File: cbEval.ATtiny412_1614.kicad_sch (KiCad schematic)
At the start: 50 parts, among them J1 Bergstik-II_3, J10 Socket.Hor.2x5.6-5535512-4, J11 Bergstik-II_3, J12 Bergstik-II_3, J13 Bergstik-II_6, J14 Bergstik-II_6, J15 Bergstik-II_6, J16 Bergstik-II_3, J17 Bergstik-II_6, J18 Bergstik-II_3, J19 Bergstik-II_6, J2 Bergstik-II_6, J20 Bergstik-II_3, J21 Bergstik-II_3, J22 Bergstik-II_2, J23 Bergstik-II_2, J3 Keystone.4918, J4 Keystone.4918, J5 Keystone.3571, J6 Keystone.3571, J7 Socket.Hor.2x5.6-5535512-4, J8 Header.Hor.2x5.9-103326-0-05, J9 Header.Hor.2x5.9-103326-0-05, U1 ATtiny412-SSFR, U2 ATtiny1614-SSFR

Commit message: kleinere Änderungen
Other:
- moved on the sheet: J23
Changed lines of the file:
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@@
   (junction (at 238.76 129.54) (diameter 0.9144) (color 0 0 0 0))
   (junction (at 251.46 50.8) (diameter 0.9144) (color 0 0 0 0))
-  (junction (at 266.7 144.78) (diameter 0.9144) (color 0 0 0 0))
   (junction (at 274.32 144.78) (diameter 0.9144) (color 0 0 0 0))
   (no_connect (at 68.58 17.78))
@@
     (stroke (width 0) (type solid) (color 0 0 0 0))
   )
+  (wire (pts (xy 137.16 99.06) (xy 127 99.06))
+    (stroke (width 0) (type solid) (color 0 0 0 0))
+  )
+  (wire (pts (xy 137.16 101.6) (xy 137.16 99.06))
+    (stroke (width 0) (type solid) (color 0 0 0 0))
+  )
   (wire (pts (xy 139.7 35.56) (xy 139.7 38.1))
     (stroke (width 0) (type solid) (color 0 0 0 0))
@@
     (stroke (width 0) (type solid) (color 0 0 0 0))
   )
-  (wire (pts (xy 139.7 99.06) (xy 127 99.06))
+  (wire (pts (xy 139.7 99.06) (xy 149.86 99.06))
     (stroke (width 0) (type solid) (color 0 0 0 0))
   )
@@
     (stroke (width 0) (type solid) (color 0 0 0 0))
   )
-  (wire (pts (xy 142.24 99.06) (xy 149.86 99.06))
-    (stroke (width 0) (type solid) (color 0 0 0 0))
-  )
-  (wire (pts (xy 142.24 101.6) (xy 142.24 99.06))
-    (stroke (width 0) (type solid) (color 0 0 0 0))
-  )
   (wire (pts (xy 147.32 165.1) (xy 154.94 165.1))
     (stroke (width 0) (type solid) (color 0 0 0 0))
@@
     (stroke (width 0) (type solid) (color 0 0 0 0))
   )
-  (wire (pts (xy 264.16 144.78) (xy 266.7 144.78))
-    (stroke (width 0) (type solid) (color 0 0 0 0))
-  )
   (wire (pts (xy 266.7 144.78) (xy 274.32 144.78))
     (stroke (width 0) (type solid) (color 0 0 0 0))
@@
     (stroke (width 0) (type solid) (color 0 0 0 0))
   )
-  (wire (pts (xy 274.32 147.32) (xy 274.32 144.78))
+  (wire (pts (xy 274.32 144.78) (xy 274.32 147.32))
     (stroke (width 0) (type solid) (color 0 0 0 0))
   )
@@
     (pin "2")
   )
-  (symbol (lib_id "J.PinHeader:Bergstik-II_2") (at 142.24 106.68 90) (mirror x) (unit 1)
-    (in_bom yes) (on_board yes)
-    (property "Reference" "J23" (id 0) (at 142.24 121.92 90))
-    (property "Value" "Bergstik-II_2" (id 1) (at 142.24 119.38 90))
-    (property "Footprint" "Connector_PinHeader_2.54mm:PinHeader_1x02_P2.54mm_Vertical" (id 2) (at 139.7 114.3 90)
-      (effects (font (size 1.27 1.27)) hide)
-    )
-    (property "Datasheet" "https://cdn.amphenol-icc.com/media/wysiwyg/files/drawing/68000.pdf?__cf_chl_jschl_tk__=264da0a199af1bdefb04026963ad3c85a073036f-1615910483-0-AaX8LtgG8apEDzGIqgzQ0aoAKWkj50oj4JyeD-4a-BjpVTotUkz0b9CwK48SctxW9RfQ29uHK-g8U4Q7W950UfkLI47M2h-zbxXP0QVGLOROToQCZGWcFC-c_QilEUacZTRKDvvL4FAsQqyycsf3m4Eg-isf3_QP12ONd_wWQcMNK-LuQ3eyU0ZB_uGz-1tHBPJYyv3B6ZQ-xQw3v8oWI_eE_zzEWbIWrLFoFf6eZXoAoT5Y4wJiyDXoV-vBmq5F4mSG8H7EqnWkU4EpxDA2-swokem-Q60MTknd4E9RK0nSmJU_PhEDac0Sb3Im75HD1QHXcTu1yMJzQCNpgpofH-wmgz79VfPk4ttpW38ZPDdPIxv_B7gR4gWWdhvgQyW6byYqLE8E5a8tpA31lZkCN19ufDO8SqP6UAFJscCeeydKEgOe2Ksu_LJQubib6v3-6A" (id 3) (at 139.7 116.84 90)
-      (effects (font (size 1.27 1.27)) hide)
-    )
-    (property "Package" "1x2-2.54" (id 4) (at 142.24 116.84 90))
-    (property "Usage" "LEDs" (id 5) (at 142.24 114.3 90))
-    (property "ID" "68000-102HLF" (id 6) (at 140.97 110.49 90)
-      (effects (font (size 0.635 0.635)))
-    )
+  (symbol (lib_id "J.PinHeader:Bergstik-II_2") (at 139.7 106.68 90) (mirror x) (unit 1)
+    (in_bom yes) (on_board yes)
+    (property "Reference" "J23" (id 0) (at 139.7 121.92 90))
+    (property "Value" "Bergstik-II_2" (id 1) (at 139.7 119.38 90))
+    (property "Footprint" "Connector_PinHeader_2.54mm:PinHeader_1x02_P2.54mm_Vertical" (id 2) (at 137.16 114.3 90)
+      (effects (font (size 1.27 1.27)) hide)
+    )
+    (property "Datasheet" "https://cdn.amphenol-icc.com/media/wysiwyg/files/drawing/68000.pdf?__cf_chl_jschl_tk__=264da0a199af1bdefb04026963ad3c85a073036f-1615910483-0-AaX8LtgG8apEDzGIqgzQ0aoAKWkj50oj4JyeD-4a-BjpVTotUkz0b9CwK48SctxW9RfQ29uHK-g8U4Q7W950UfkLI47M2h-zbxXP0QVGLOROToQCZGWcFC-c_QilEUacZTRKDvvL4FAsQqyycsf3m4Eg-isf3_QP12ONd_wWQcMNK-LuQ3eyU0ZB_uGz-1tHBPJYyv3B6ZQ-xQw3v8oWI_eE_zzEWbIWrLFoFf6eZXoAoT5Y4wJiyDXoV-vBmq5F4mSG8H7EqnWkU4EpxDA2-swokem-Q60MTknd4E9RK0nSmJU_PhEDac0Sb3Im75HD1QHXcTu1yMJzQCNpgpofH-wmgz79VfPk4ttpW38ZPDdPIxv_B7gR4gWWdhvgQyW6byYqLE8E5a8tpA31lZkCN19ufDO8SqP6UAFJscCeeydKEgOe2Ksu_LJQubib6v3-6A" (id 3) (at 137.16 116.84 90)
+      (effects (font (size 1.27 1.27)) hide)
+    )
+    (property "Package" "1x2-2.54" (id 4) (at 139.7 116.84 90))
+    (property "Usage" "LEDs" (id 5) (at 139.7 114.3 90))
+    (property "ID" "68000-102HLF" (id 6) (at 138.43 110.49 90)
+      (effects (font (size 0.635 0.635)))
+    )

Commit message: BOM erstellt und kleinere Korrekturen
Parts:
- added R10, R11, R12, R13, R14, R15, R9: 10k, Resistor_SMD:R_0805_2012Metric, symbol R.Yageo.RC0805:10k
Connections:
- net GND: now also R10.2, R11.2, R12.2, R13.2, R14.2, R9.2
- net SPI-ADR0: now also R9.1
- net SPI-ADR1: now also R10.1
- net SPI-ADR2: now also R11.1
- net SPI-CLK: now also R14.1
- net SPI-MRST: now also R13.1
- net SPI-MTSR: now also R12.1
- net SPI-~CE: now also R15.2
- net VCC: now also R15.1
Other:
- moved on the sheet: D1A, D1B, H2, H3, J10, J13, J22, J23, R5, R6, R7, R8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

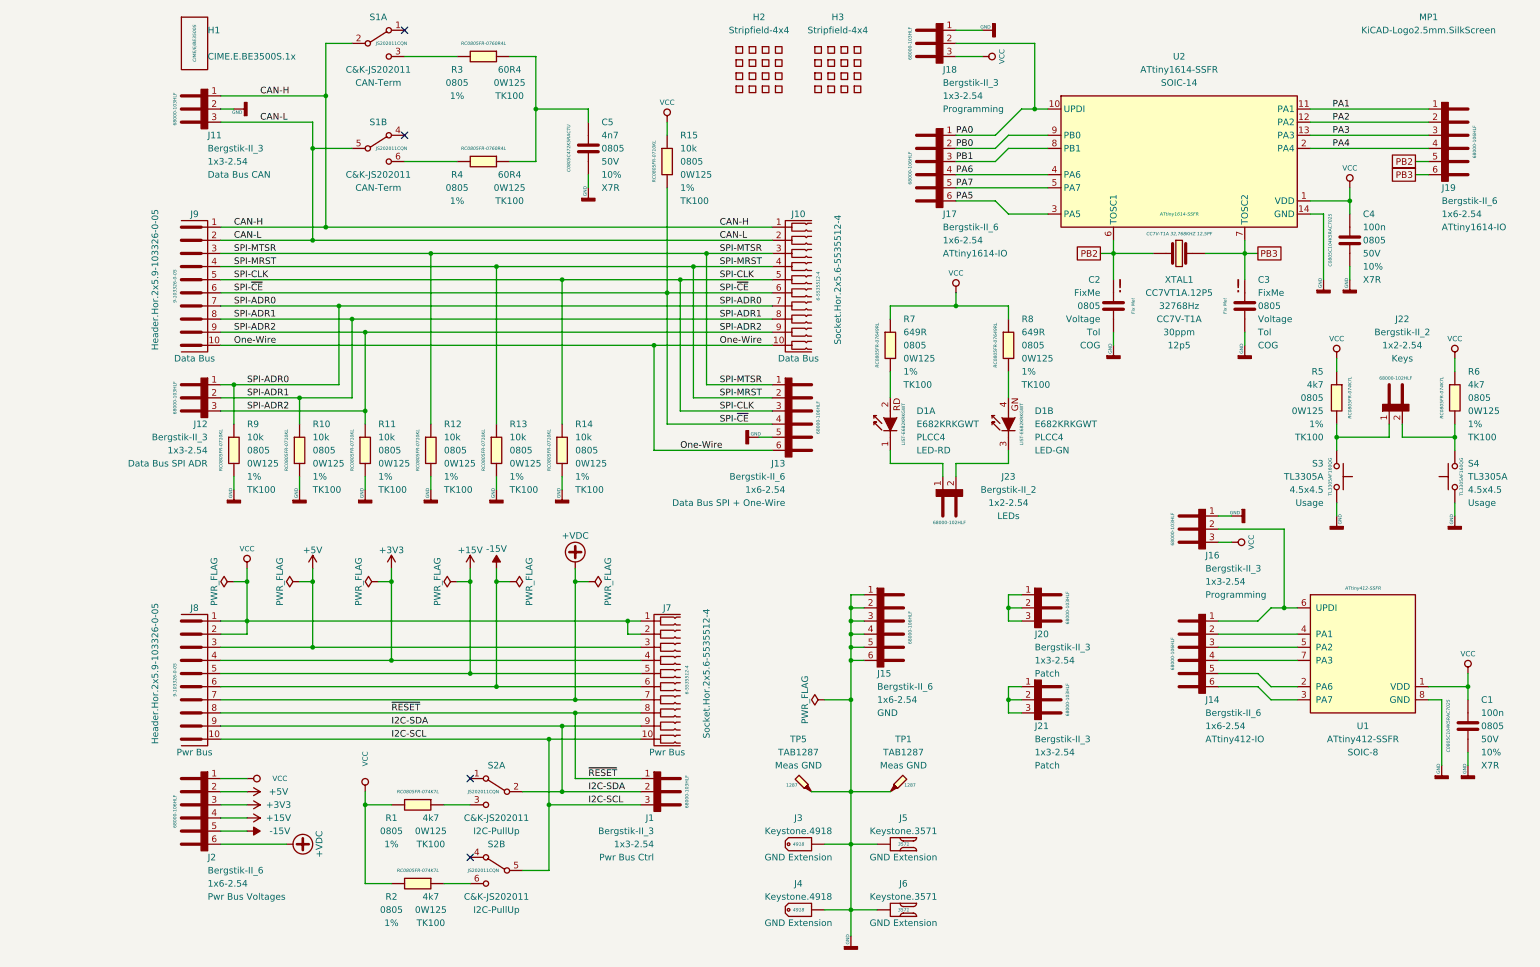
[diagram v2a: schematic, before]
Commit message: Bus-Stecker ersetzt, Poti hinzugefügt
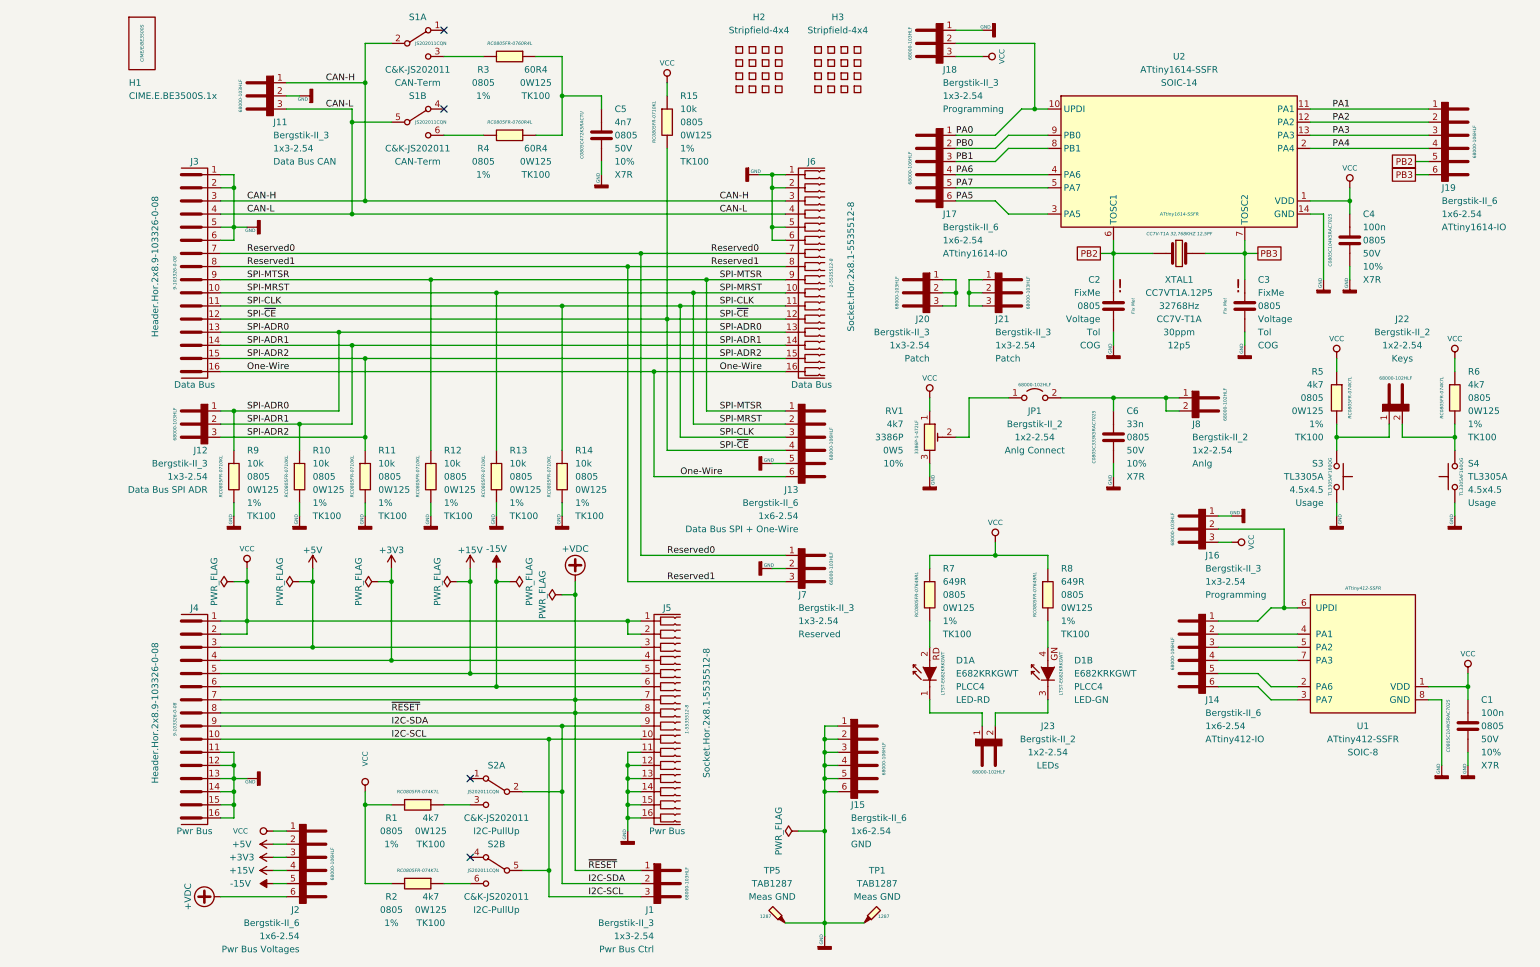
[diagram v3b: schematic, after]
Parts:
- removed J10, J7: Socket.Hor.2x5.6-5535512-4, BTech.Connector.AMPMODU-ModII:Socket.Hor.2x5.6-5535512-4, symbol J.AMPMODU-ModII:Socket.Hor.2x5.6-5535512-4
- removed J3, J4: Keystone.4918, BTech.Connector.QuickConnect:Keystone.4918, symbol J.QuickConnect:Keystone.4918
- removed J5, J6: Keystone.3571, BTech.Connector.QuickConnect:Keystone.3571, symbol J.QuickConnect:Keystone.3571
- removed J8, J9: Header.Hor.2x5.9-103326-0-05, Connector_PinHeader_2.54mm:PinHeader_2x05_P2.54mm_Horizontal, symbol J.AMPMODU-ModII:Header.Hor.2x5.9-103326-0-05
- removed MP1: KiCAD-Logo2.5mm.SilkScreen, Symbol:KiCad-Logo2_5mm_SilkScreen, symbol Symbol:KiCAD-Logo2.5mm.SilkScreen
- added C6: 33n, Capacitor_SMD:C_0805_2012Metric, symbol C.Kemet.MLCC.0805.X7R:33n
- added J3, J4: Header.Hor.2x8.9-103326-0-08, Connector_PinHeader_2.54mm:PinHeader_2x08_P2.54mm_Horizontal, symbol J.AMPMODU-ModII:Header.Hor.2x8.9-103326-0-08
- added J5, J6: Socket.Hor.2x8.1-5535512-8, BTech.Connector.AMPMODU-ModII:Socket.Hor.2x5.6-5535512-4, symbol J.AMPMODU-ModII:Socket.Hor.2x8.1-5535512-8
- added J7: Bergstik-II_3, Connector_PinHeader_2.54mm:PinHeader_1x03_P2.54mm_Vertical, symbol J.PinHeader:Bergstik-II_3
- added J8: Bergstik-II_2, Connector_PinHeader_2.54mm:PinHeader_1x02_P2.54mm_Vertical, symbol J.PinHeader:Bergstik-II_2
- added JP1: Bergstik-II_2, Connector_PinHeader_2.54mm:PinHeader_1x02_P2.54mm_Vertical, symbol JP:Bergstik-II_2
- added RV1: 4k7, Potentiometer_THT:Potentiometer_Bourns_3386P_Vertical, symbol RV.Bourns.3386P:4k7
- D1: ID LIST-E682KRKGWT -> LTST-E682KRKGWT
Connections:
- net ~RESET is gone; now on net +VDC: J1.1 (A1)
- net +15V: now also J4.5, J5.5
- net +3V3: now also J4.4, J5.4
- net +5V: now also J4.3, J5.3
- net +VDC: now also J4.7, J4.8, J5.7, J5.8
- net -15V: now also J4.6, J5.6
- net CAN-H: now also J3.3, J6.3
- net CAN-L: now also J3.4, J6.4
- net GND: now also C6.2, J3.1, J3.2, J3.5, J3.6, J4.11, J4.12, J4.13, J4.14, J4.15, J4.16, J5.11, J5.12, J5.13, J5.14, J5.15, J5.16, J6.1, J6.2, J6.5, J6.6, J7.2 (A2), RV1.3
- net I2C-SCL: now also J4.10, J5.10
- net I2C-SDA: now also J4.9, J5.9
- net One-Wire: now also J3.16, J6.16
- net SPI-ADR0: now also J3.13, J6.13
- net SPI-ADR1: now also J3.14, J6.14
- net SPI-ADR2: now also J3.15, J6.15
- net SPI-CLK: now also J3.11, J6.11
- net SPI-MRST: now also J3.10, J6.10
- net SPI-MTSR: now also J3.9, J6.9
- net SPI-~CE: now also J3.12, J6.12
- net VCC: now also J4.1, J4.2, J5.1, J5.2, RV1.1
- new net: JP1.1 (A), RV1.2
- new net: C6.1, J8.1 (A1), J8.2 (A2), JP1.2 (B)
- new net Reserved0: J3.7, J6.7, J7.1 (A1)
- new net Reserved1: J3.8, J6.8, J7.3 (A3)
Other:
- moved on the sheet: C5, D1A, D1B, H1, J1, J11, J12, J13, J15, J2, J20, J21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

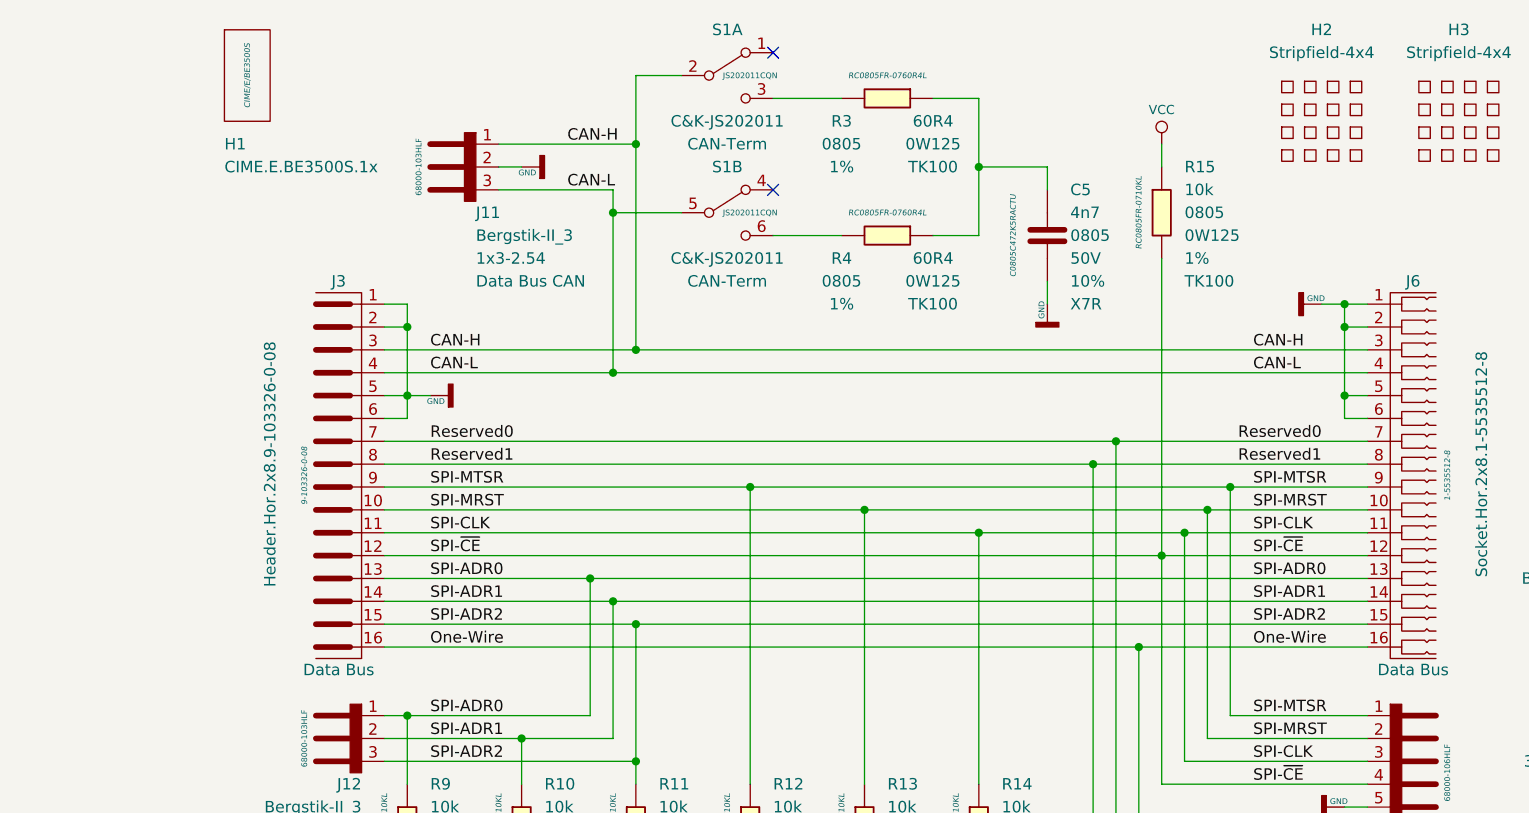
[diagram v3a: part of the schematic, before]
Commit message: 1Wire-Terminierung hinzugefügt, BOM erneuert
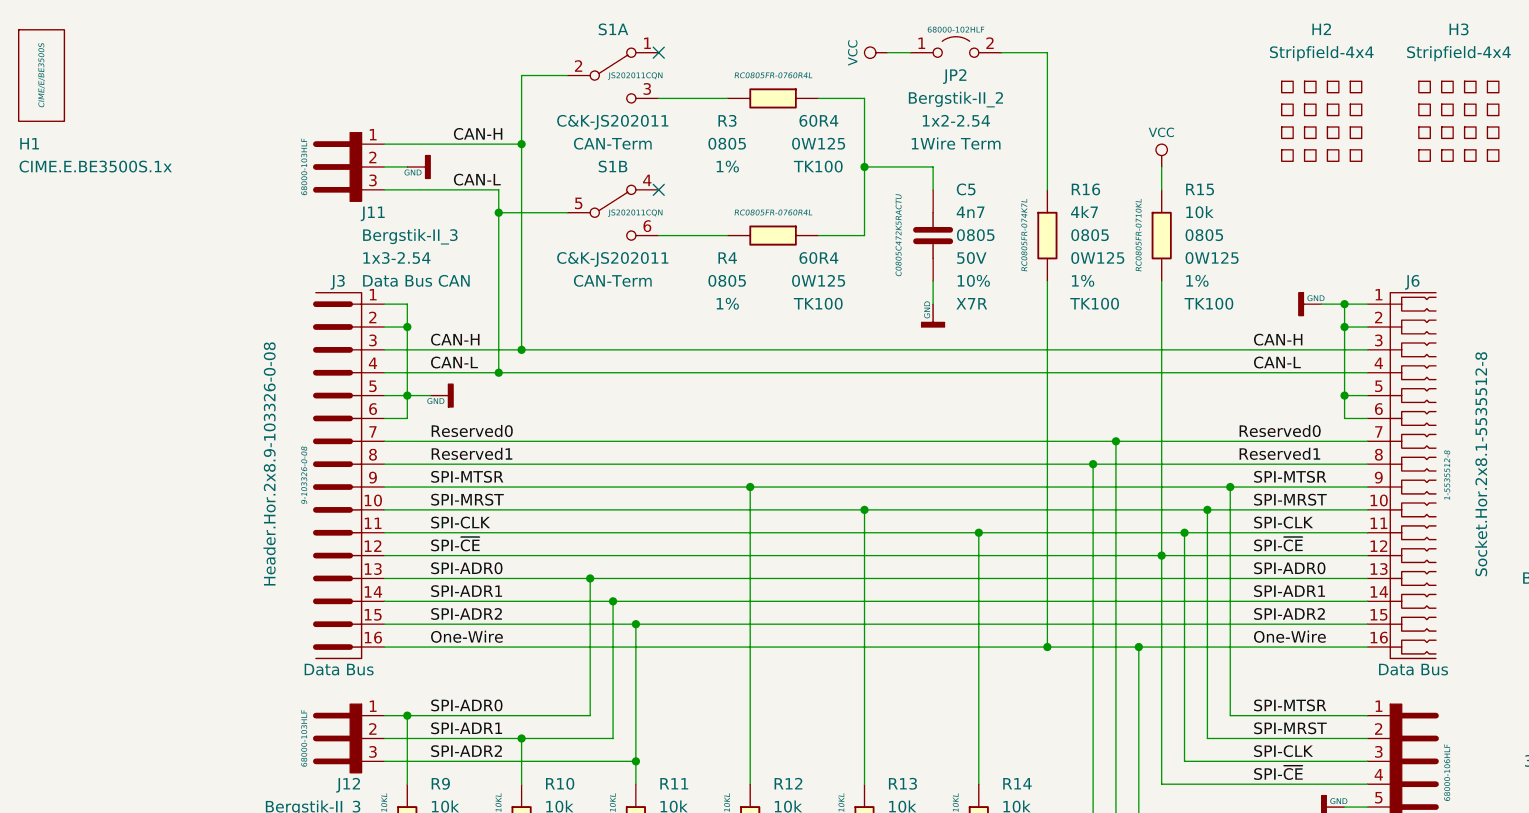
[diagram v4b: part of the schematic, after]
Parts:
- added JP2: Bergstik-II_2, Connector_PinHeader_2.54mm:PinHeader_1x02_P2.54mm_Vertical, symbol JP:Bergstik-II_2
- added R16: 4k7, Resistor_SMD:R_0805_2012Metric, symbol R.Yageo.RC0805:4k7
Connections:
- net One-Wire: now also R16.2
- net VCC: now also JP2.1 (A)
- new net: JP2.2 (B), R16.1
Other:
- moved on the sheet: C5, H1, J11, R15, R3, R4, S1A, S1B
